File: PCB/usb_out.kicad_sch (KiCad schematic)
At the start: 6 parts, among them J3 USB_A

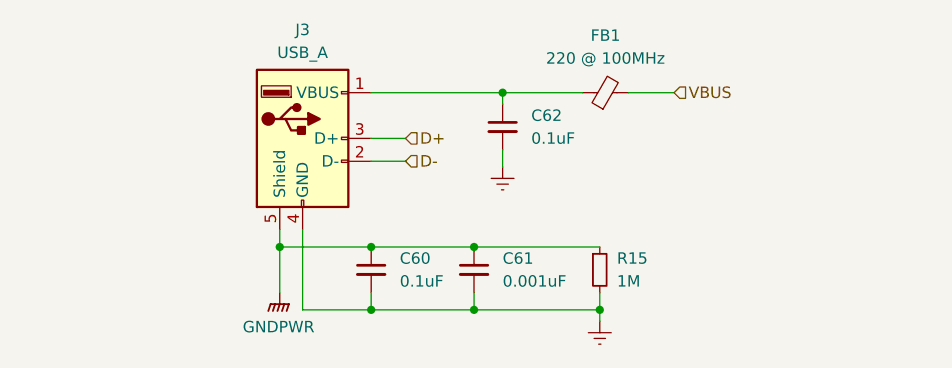
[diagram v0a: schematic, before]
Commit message: comply with ERC
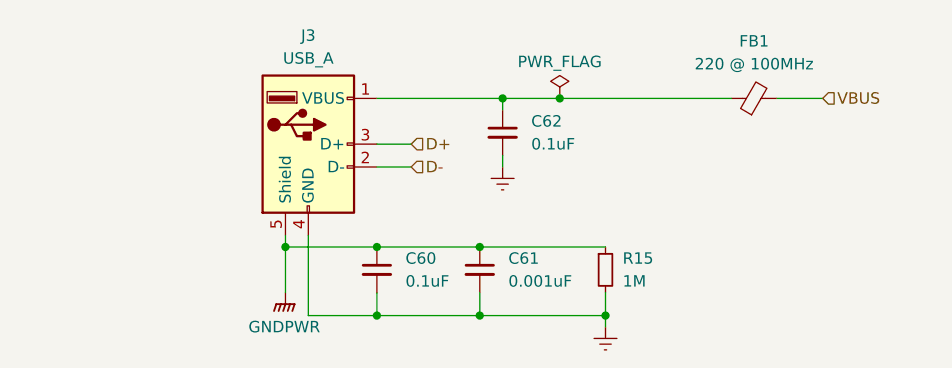
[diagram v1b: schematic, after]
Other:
- moved on the sheet: C60, C61, C62, FB1, J3, R15

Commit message: add net classes
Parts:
- renumbered C60 to C72, C61 to C73, C62 to C74, FB1 to FB7, J3 to J7, R15 to R19

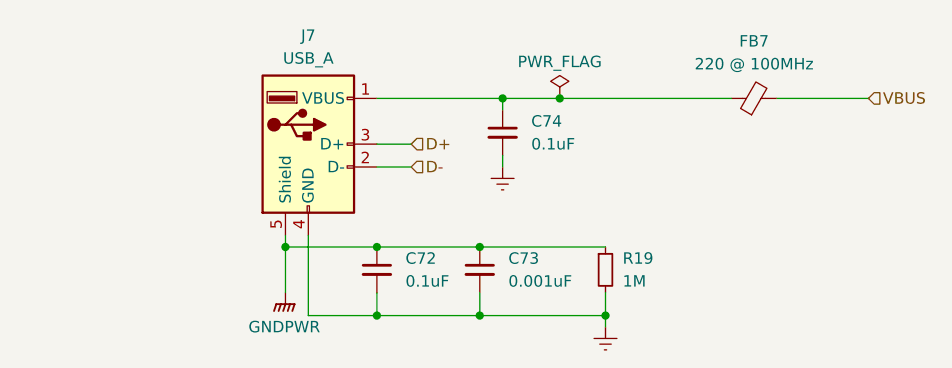
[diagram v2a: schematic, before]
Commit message: adjust schematic to match real components, assign footprints
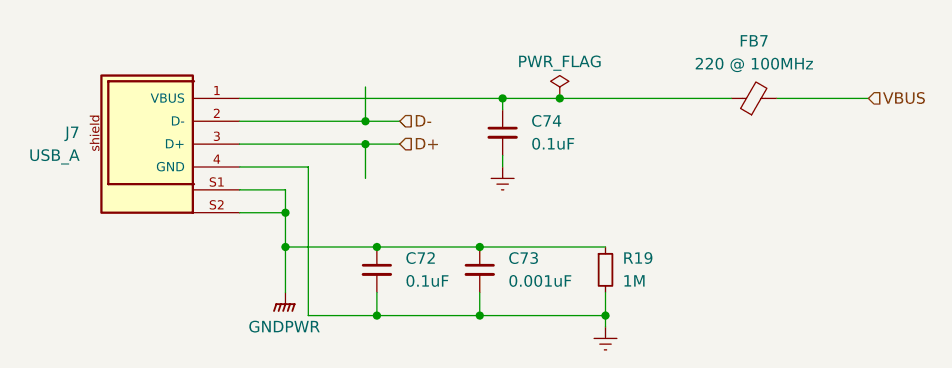
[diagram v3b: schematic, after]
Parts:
- C72, C73, C74: footprint (none) -> Capacitor_SMD:C_0402_1005Metric
- FB7: footprint (none) -> my_global:BEADC1608X95N
- J7: footprint (none) -> my_global:61400416021; symbol Connector:USB_A -> 61400416021:61400416021
- R19: footprint (none) -> Resistor_SMD:R_0402_1005Metric
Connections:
- net GNDPWR: now also J7.S1, J7.S2; no longer J7.5 (Shield)
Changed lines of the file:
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@@
+	)
+	(junction
+		(at 87.63 71.12)
+		(diameter 0)
+		(color 0 0 0 0)
 	)
 	(junction
@@
 	)
 	(junction
+		(at 96.52 60.96)
+		(diameter 0)
+		(color 0 0 0 0)
+	)
+	(junction
 		(at 87.63 74.93)
 		(diameter 0)
@@
 		(color 0 0 0 0)
 	)
-	(wire
-		(pts
-			(xy 97.79 58.42) (xy 111.76 58.42)
+	(junction
+		(at 96.52 63.5)
+		(diameter 0)
+		(color 0 0 0 0)
+	)
+	(wire
+		(pts
+			(xy 96.52 57.15) (xy 96.52 60.96)
 		)
 		(stroke
@@
 	(wire
 		(pts
+			(xy 87.63 71.12) (xy 87.63 74.93)
+		)
+		(stroke
+			(width 0)
+			(type default)
+		)
+	)
+	(wire
+		(pts
+			(xy 82.55 60.96) (xy 96.52 60.96)
+		)
+		(stroke
+			(width 0)
+			(type default)
+		)
+	)
+	(wire
+		(pts
+			(xy 90.17 66.04) (xy 90.17 82.55)
+		)
+		(stroke
+			(width 0)
+			(type default)
+		)
+	)
+	(wire
+		(pts
 			(xy 111.76 58.42) (xy 118.11 58.42)
 		)
@@
 	(wire
 		(pts
-			(xy 97.79 66.04) (xy 101.6 66.04)
+			(xy 82.55 71.12) (xy 87.63 71.12)
 		)
 		(stroke
@@
 	(wire
 		(pts
+			(xy 82.55 68.58) (xy 87.63 68.58)
+		)
+		(stroke
+			(width 0)
+			(type default)
+		)
+	)
+	(wire
+		(pts
+			(xy 96.52 63.5) (xy 100.33 63.5)
+		)
+		(stroke
+			(width 0)
+			(type default)
+		)
+	)
+	(wire
+		(pts
 			(xy 142.24 58.42) (xy 152.4 58.42)
 		)
@@
 	(wire
 		(pts
+			(xy 82.55 58.42) (xy 111.76 58.42)
+		)
+		(stroke
+			(width 0)
+			(type default)
+		)
+	)
+	(wire
+		(pts
 			(xy 111.76 64.77) (xy 111.76 66.04)
 		)
@@
 	(wire
 		(pts
-			(xy 87.63 73.66) (xy 87.63 74.93)
+			(xy 87.63 68.58) (xy 87.63 71.12)
+		)
+		(stroke
+			(width 0)
+			(type default)
+		)
+	)
+	(wire
+		(pts
+			(xy 82.55 63.5) (xy 96.52 63.5)
+		)
+		(stroke
+			(width 0)
+			(type default)
+		)
+	)
+	(wire
+		(pts
+			(xy 90.17 66.04) (xy 82.55 66.04)
 		)
 		(stroke
@@
 	(wire
 		(pts
-			(xy 97.79 63.5) (xy 101.6 63.5)
-		)
-		(stroke
-			(width 0)
-			(type default)
-		)
-	)
-	(wire
-		(pts
 			(xy 123.19 82.55) (xy 123.19 83.82)
 		)
@@
 	(wire
 		(pts
-			(xy 90.17 73.66) (xy 90.17 82.55)
+			(xy 96.52 67.31) (xy 96.52 63.5)
+		)
+		(stroke
+			(width 0)
+			(type default)
+		)
+	)
+	(wire
+		(pts
+			(xy 96.52 60.96) (xy 100.33 60.96)
 		)
 		(stroke
@@
 	(hierarchical_label "D+"
 		(shape input)
-		(at 101.6 63.5 0)
+		(at 100.33 63.5 0)
 		(effects
 			(font
@@
 	(hierarchical_label "D-"
 		(shape input)
-		(at 101.6 66.04 0)
+		(at 100.33 60.96 0)
 		(effects
 			(font
@@
 		(length 2.54)
 		(shape round)
-		(at 97.79 63.5 0)
+		(at 96.52 67.31 180)
 		(fields_autoplaced yes)
 		(effects
@@
 				(size 1.27 1.27)
 			)
-			(justify left bottom)
+			(justify right bottom)
 		)
 		(property "Netclass" "HIGH SPEED"
-			(at 98.4885 60.96 0)
+			(at 97.2185 69.85 0)
 			(effects
 				(font
@@
 		)
 		(property "Component Class" ""
-			(at -57.15 6.35 0)
+			(at -58.42 10.16 0)
 			(effects
 				(font
@@
 		(length 2.54)
 		(shape round)
-		(at 97.79 66.04 180)
+		(at 96.52 57.15 0)
 		(fields_autoplaced yes)
 		(effects
@@
 				(size 1.27 1.27)
 			)
-			(justify right bottom)
+			(justify left bottom)
 		)
 		(property "Netclass" "HIGH SPEED"
-			(at 98.4885 68.58 0)
+			(at 97.2185 54.61 0)
 			(effects
 				(font
@@
 		)
 		(property "Component Class" ""
-			(at -57.15 8.89 0)
+			(at -58.42 0 0)
 			(effects
 				(font
@@
 			)
 		)
-		(property "Footprint" ""
+		(property "Footprint" "my_global:BEADC1608X95N"
 			(at 139.7 60.198 90)
 			(effects
@@
 			)
 		)
-		(property "Footprint" ""
+		(property "Footprint" "Resistor_SMD:R_0402_1005Metric"
 			(at 123.19 77.47 0)
 			(effects
@@
 			)
 		)
-		(property "Footprint" ""
+		(property "Footprint" "Capacitor_SMD:C_0402_1005Metric"
 			(at 97.79 77.47 0)
 			(effects
@@
 			)
 		)
-		(property "Footprint" ""
+		(property "Footprint" "Capacitor_SMD:C_0402_1005Metric"
 			(at 109.22 77.47 0)
 			(effects
@@
 	)
 	(symbol
-		(lib_id "Connector:USB_A")
-		(at 90.17 63.5 0)
+		(lib_id "61400416021:61400416021")
+		(at 72.39 60.96 0)
+		(mirror y)
 		(unit 1)
 		(exclude_from_sim no)
@@
 		(on_board yes)
 		(dnp no)
-		(fields_autoplaced yes)
 		(property "Reference" "J7"
-			(at 90.17 51.435 0)
-			(effects
-				(font
-					(size 1.27 1.27)
-				)
+			(at 64.77 62.2299 0)
+			(effects
+				(font
+					(size 1.27 1.27)
+				)
+				(justify left)
 			)
 		)
 		(property "Value" "USB_A"
-			(at 90.17 53.975 0)
-			(effects
-				(font
-					(size 1.27 1.27)
-				)
-			)
-		)
-		(property "Footprint" ""
-			(at 93.98 64.77 0)
-			(effects
-				(font
-					(size 1.27 1.27)
-				)
+			(at 64.77 64.7699 0)
+			(effects
+				(font
+					(size 1.27 1.27)
+				)
+				(justify left)
+			)
+		)
+		(property "Footprint" "my_global:61400416021"
+			(at 72.39 60.96 0)
+			(effects
+				(font
+					(size 1.27 1.27)
+				)
+				(justify bottom)
 				(hide yes)
 			)
 		)
 		(property "Datasheet" " ~"
-			(at 93.98 64.77 0)
+			(at 72.39 60.96 0)
 			(effects
 				(font
@@
 		)
 		(property "Description" ""
-			(at 90.17 63.5 0)
-			(effects
-				(font
-					(size 1.27 1.27)
-				)
+			(at 72.39 60.96 0)
+			(effects
+				(font
+					(size 1.27 1.27)
+				)
+				(hide yes)
 			)
 		)
@@
 		(pin "4"
 		)
-		(pin "5"
+		(pin "S2"
+		)
+		(pin "S1"
 		)
 		(instances
@@
 			)
 		)
-		(property "Footprint" ""
+		(property "Footprint" "Capacitor_SMD:C_0402_1005Metric"
 			(at 111.76 62.23 0)
 			(effects
